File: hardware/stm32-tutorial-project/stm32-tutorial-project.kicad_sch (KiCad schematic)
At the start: 49 parts, among them J2 10pin IDC SWD, J3 Conn_01x04, J4 Conn_01x04, J5 Conn_01x13, J6 Conn_01x13, Q1 NPN, Q3 PNP, SW1 SW_Push, SW2 SW_Push_SPDT, U1 STM32G431CBTx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

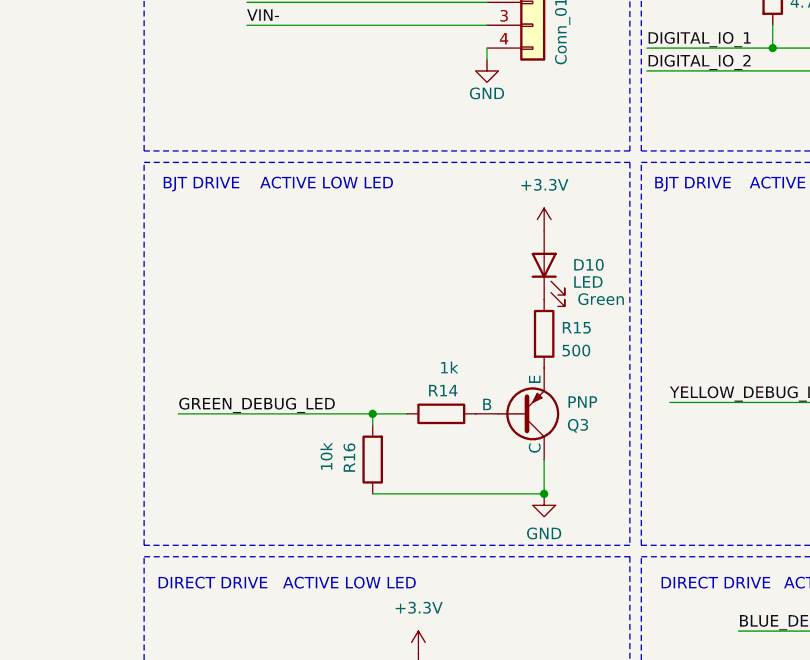
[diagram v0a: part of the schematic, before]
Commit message: Correct PNP LED driver to match NPN behaviour per #1
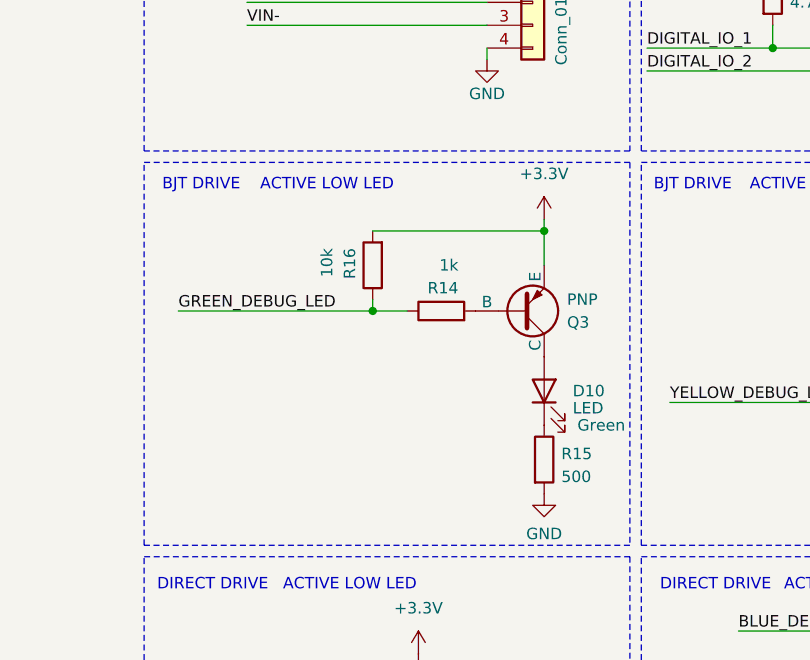
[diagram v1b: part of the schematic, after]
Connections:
- net +3.3V: now also Q3.3 (E), R16.2; no longer D10.2 (A)
- net GND: now also R15.2; no longer Q3.1 (C), R16.1
- net GREEN_DEBUG_LED: now also R16.1; no longer R16.2
- new net: D10.2 (A), Q3.1 (C)
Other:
- moved on the sheet: D10, Q3, R14, R15, R16

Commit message: Add missing connectors, test points, and jumpers
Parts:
- J5, J6: footprint (none) -> Connector_PinHeader_2.54mm:PinHeader_1x13_P2.54mm_Vertical
- JP1: footprint (none) -> Jumper:SolderJumper-3_P1.3mm_Open_Pad1.0x1.5mm_NumberLabels
- JP4: footprint (none) -> Connector_PinHeader_2.54mm:PinHeader_1x03_P2.54mm_Vertical
- JP5: footprint (none) -> Connector_PinHeader_2.54mm:PinHeader_1x02_P2.54mm_Vertical
- TP1, TP2: footprint (none) -> TestPoint:TestPoint_Pad_D3.0mm
- renumbered R_EXT to R_EXT1
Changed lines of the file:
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@@
 			)
 		)
-		(property "Footprint" ""
+		(property "Footprint" "TestPoint:TestPoint_Pad_D3.0mm"
 			(at 262.255 76.2 0)
 			(effects
@@
 			)
 		)
-		(property "Footprint" ""
+		(property "Footprint" "Connector_PinHeader_2.54mm:PinHeader_1x13_P2.54mm_Vertical"
 			(at 194.31 34.29 0)
 			(effects
@@
 			)
 		)
-		(property "Footprint" ""
+		(property "Footprint" "Connector_PinHeader_2.54mm:PinHeader_1x02_P2.54mm_Vertical"
 			(at 257.81 62.23 0)
 			(effects
@@
 			)
 		)
-		(property "Footprint" ""
+		(property "Footprint" "Connector_PinHeader_2.54mm:PinHeader_1x13_P2.54mm_Vertical"
 			(at 217.17 34.29 0)
 			(effects
@@
 			)
 		)
-		(property "Footprint" ""
+		(property "Footprint" "Jumper:SolderJumper-3_P1.3mm_Open_Pad1.0x1.5mm_NumberLabels"
 			(at 107.95 57.15 0)
 			(effects
@@
 		(on_board yes)
 		(dnp no)
-		(property "Reference" "R_EXT"
+		(property "Reference" "R_EXT1"
 			(at 58.42 81.28 90)
 			(effects
@@
 			(project "stm32-tutorial-project"
 				(path "/d669673b-e709-4a82-ac8c-4eb3d8c60d0b"
-					(reference "R_EXT")
+					(reference "R_EXT1")
 					(unit 1)
 				)
@@
 			)
 		)
-		(property "Footprint" ""
+		(property "Footprint" "TestPoint:TestPoint_Pad_D3.0mm"
 			(at 252.095 78.74 0)
 			(effects
@@
 			)
 		)
-		(property "Footprint" ""
+		(property "Footprint" "Connector_PinHeader_2.54mm:PinHeader_1x03_P2.54mm_Vertical"
 			(at 269.24 58.42 0)
 			(effects

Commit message: Correct remaining connectors, complete ratsnest now available
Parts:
- J3, J4: footprint 4ms_Connector:Pins_1x04_2.54mm_TH_SWD -> Connector_PinHeader_2.54mm:PinHeader_1x04_P2.54mm_Vertical
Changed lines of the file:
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@@
 			)
 		)
-		(property "Footprint" "4ms_Connector:Pins_1x04_2.54mm_TH_SWD"
+		(property "Footprint" "Connector_PinHeader_2.54mm:PinHeader_1x04_P2.54mm_Vertical"
 			(at 274.32 69.215 0)
 			(effects
@@
 			)
 		)
-		(property "Footprint" "4ms_Connector:Pins_1x04_2.54mm_TH_SWD"
+		(property "Footprint" "Connector_PinHeader_2.54mm:PinHeader_1x04_P2.54mm_Vertical"
 			(at 215.9 64.135 0)
 			(effects

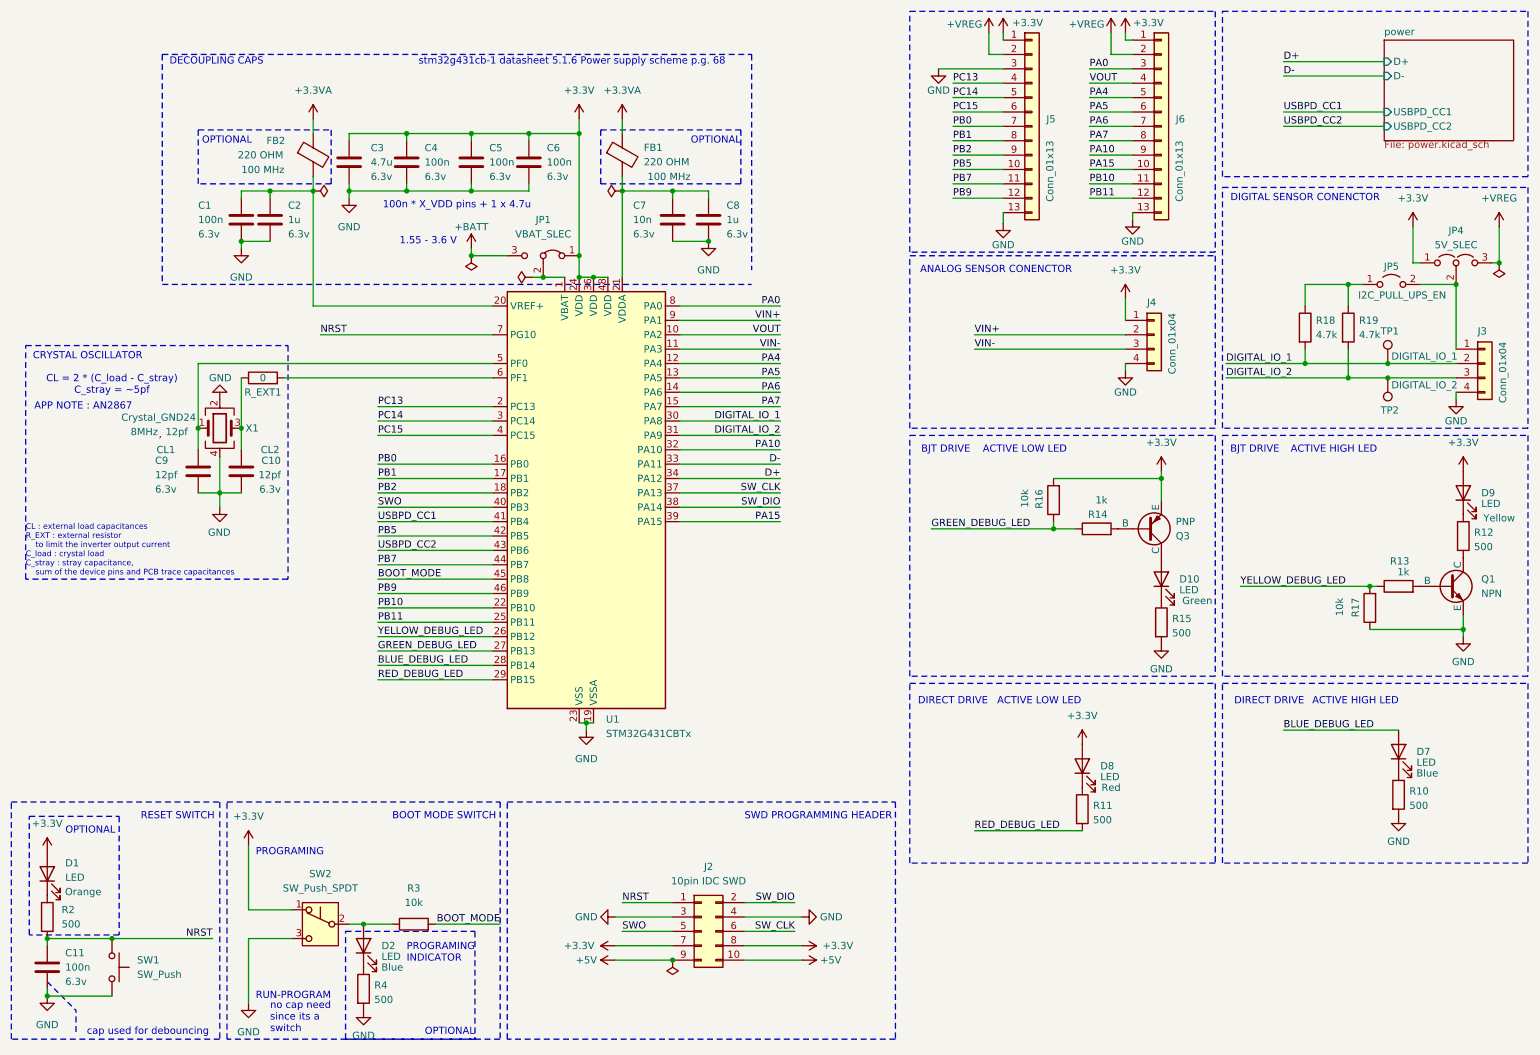
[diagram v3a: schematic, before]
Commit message: added dead battery pins to the cc lines so usbpd will work correctly
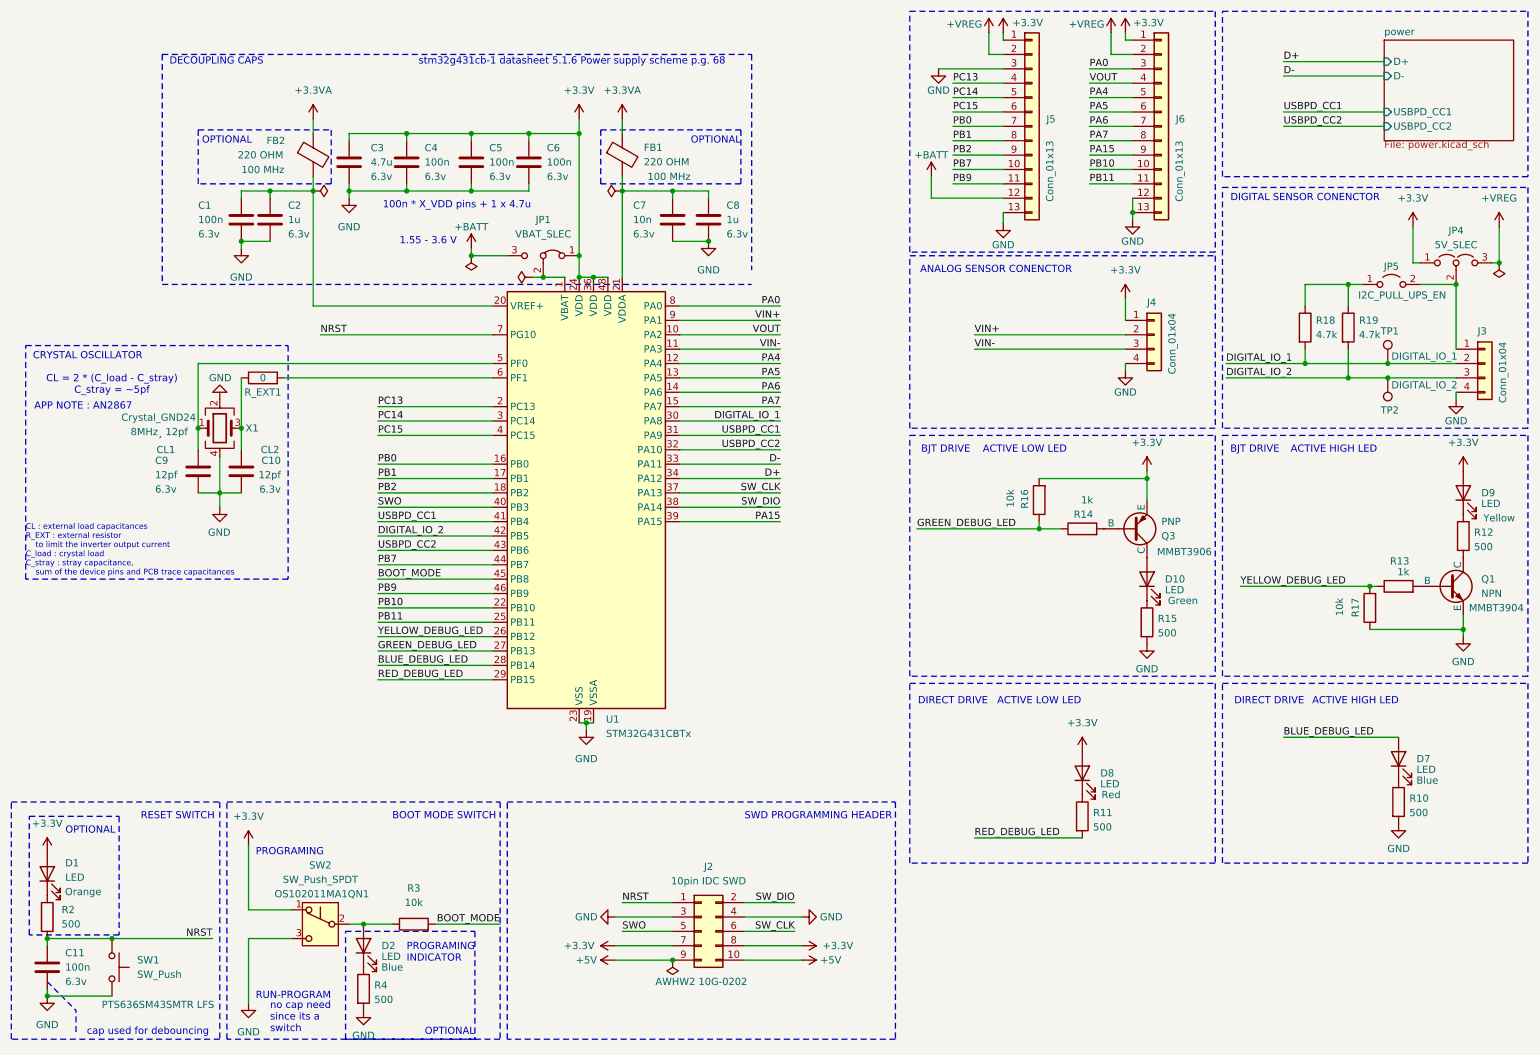
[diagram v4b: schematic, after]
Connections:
- net +BATT: now also J5.12 (Pin_12)
- net DIGITAL_IO_2: now also U1.42 (PB5); no longer U1.31 (PA9)
- net GND: now also J6.12 (Pin_12)
- net PA15: now also J6.9 (Pin_9); no longer J6.10 (Pin_10)
- net PB10: now also J6.10 (Pin_10); no longer J6.11 (Pin_11)
- net PB11: now also J6.11 (Pin_11); no longer J6.12 (Pin_12)
- net PB7: now also J5.10 (Pin_10); no longer J5.11 (Pin_11)
- net PB9: now also J5.11 (Pin_11); no longer J5.12 (Pin_12)
- net USBPD_CC1: now also U1.31 (PA9)
- net USBPD_CC2: now also U1.32 (PA10)
- removed net PA10: J6.9 (Pin_9), U1.32 (PA10)
- removed net PB5: J5.10 (Pin_10), U1.42 (PB5)
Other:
- title: (none) -> MCU
- moved on the sheet: D10, D7, D8, Q3, R10, R11, R14, R15, R16
